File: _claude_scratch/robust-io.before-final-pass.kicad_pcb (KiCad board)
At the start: 4 copper layers, 160 x 100 mm, 304 parts, among them J1 AVR-ISP-6, J10 Screw_Terminal_01x06, J14 Screw_Terminal_01x04, J15 Screw_Terminal_01x04, J16 Screw_Terminal_01x06, J18 Screw_Terminal_01x06, J19 Screw_Terminal_01x06, J20 UART, J3 Screw_Terminal_01x06, J4 Screw_Terminal_01x04, J5 Screw_Terminal_01x06, J6 Screw_Terminal_01x06, J9 Screw_Terminal_01x06, Q3 2N7002, Q4 2N7002, SW1 CHS-01TB, SW2 B3U-1000P, U1 DRV8876, U10 BTS7008, U11 BTS7008, U14 DRV8876, U2 ATmega1284P-A, U3 MCP2515, U4 TPS5604, U5 TPS5604, U6 MCP2562-E-MF, U7 MC33978, U8 BTS7008, U9 BTS7008, Y1 16MHz, Y2 12MHz

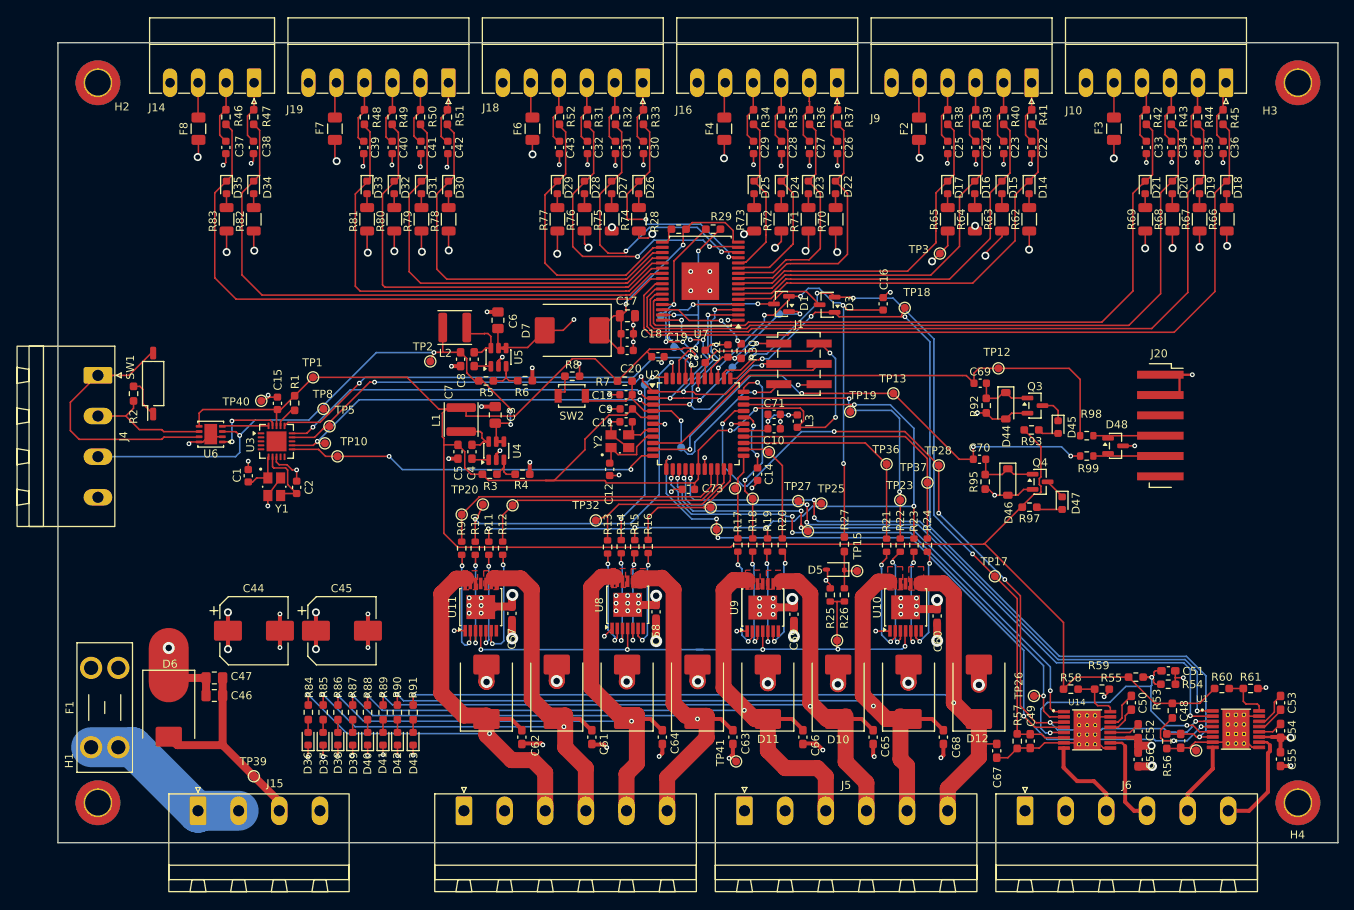
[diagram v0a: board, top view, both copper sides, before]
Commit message: Rev A: release to fab (JLCPCB, 5 PCB / 2 assembled)
Board
- Outline set to exactly 160 x 100 mm; plane zones resized to match
- UART brought out on J20 (1x6 SMD, FTDI pinout) with series
  resistors R98/R99 and TVS D48
- J1 and J20 changed to SMD headers (C52016780, C41417363)
- L1/L2 moved to Sunlord SWPA4030S footprints; regulator tracks rerouted
- 41 test points added (35 top, 6 bottom), including SPI access
- Crystal case pins (Y1/Y2 pads 2, 4) tied to GND
- SW2 changed to 2-pin push button symbol
- R84-R91 changed from 2.2k to 10k to cut dissipation at 24 V
- Thermal vias in U1/U14 enlarged to 0.3 mm drill; 27 +24V vias added
  under U8-U11; solid plane connections on high-current pins
- Input/output rows and edge connectors aligned
- /inputs/_SG4 track and via moved clear of R74 pad 1

Schematic
- ERC cleared: no-connects, PWR_FLAGs, pin types, off-grid items
- Symbols moved to project library robust-io
- Test point symbols added on processor and power sheets

Rules
- Custom DRC rule for U7 pad-to-pad clearance (0.15 mm)
- Minimum through hole 0.2 mm; silk-to-edge check ignored

Fab outputs (fab/)
- make_gerbers.sh: Gerbers, drill and position export via kicad-cli
- JLC BOM with LCSC part numbers on all 50 SMD lines
- JLC placement file with per-part rotation offsets
  (cpl_rotation_offsets.json), verified in JLC placement preview
- Through-hole BOM and test point list

DRC: 4 library-mismatch warnings (J20, U1, U14, U7), 0 errors
ERC: clean
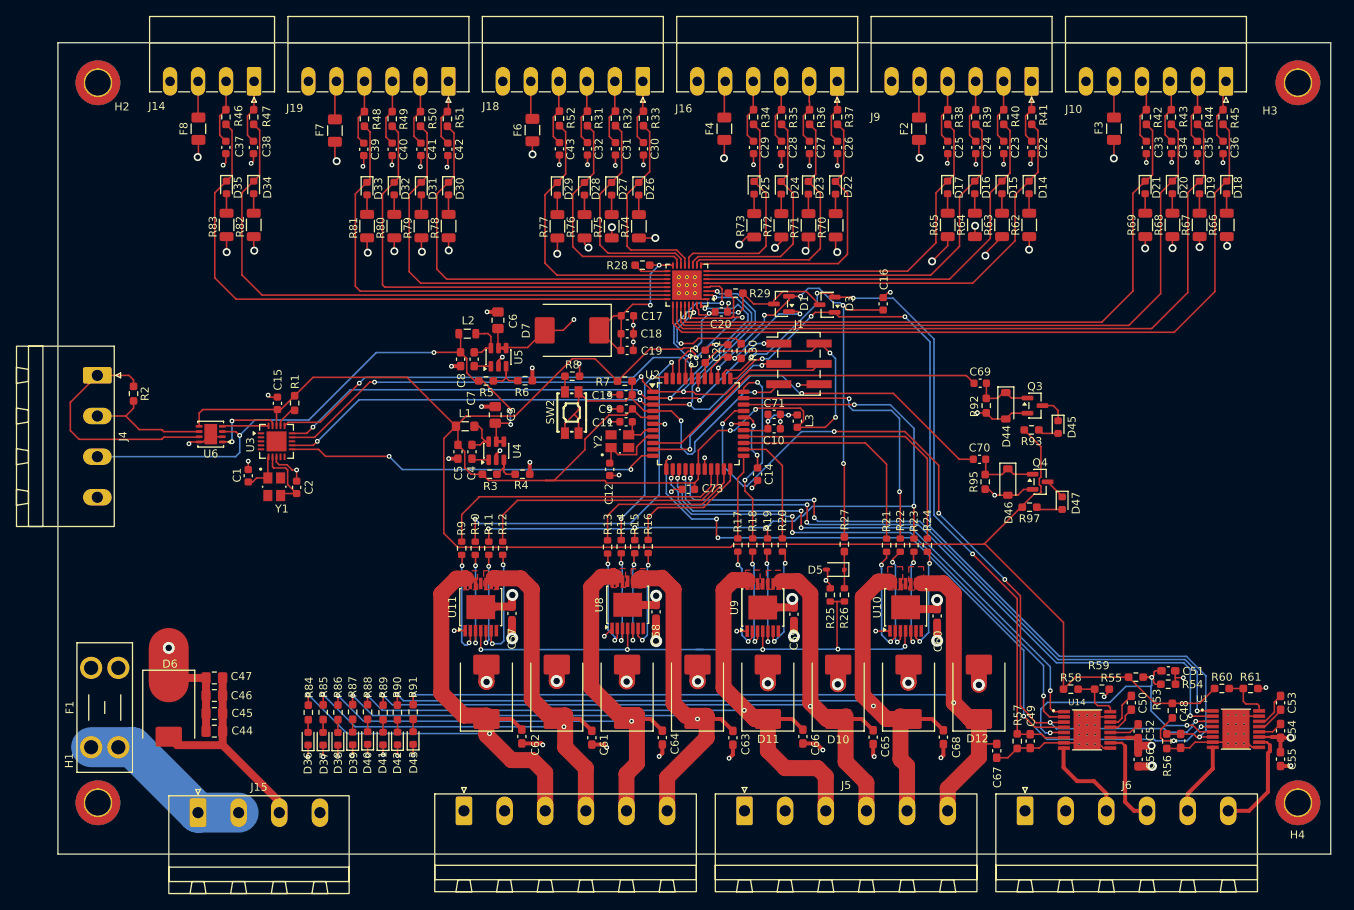
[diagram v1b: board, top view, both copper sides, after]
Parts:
- removed D48: SP0502BAHT, Package_TO_SOT_SMD:SOT-23
- removed J20: UART, Connector_PinHeader_2.54mm:PinHeader_1x06_P2.54mm_Vertical_SMD_Pin1Right
- removed R98, R99: 1k, Resistor_SMD:R_0603_1608Metric
- removed SW1: CHS-01TB, Button_Switch_SMD:SW_DIP_SPSTx01_Slide_Copal_CHS-01B_W7.62mm_P1.27mm
- removed TP1: +3.3V, TestPoint:TestPoint_Pad_D1.0mm
- removed TP10: INT_CAN0, TestPoint:TestPoint_Pad_D1.0mm
- removed TP11: RST, TestPoint:TestPoint_Pad_D1.0mm
- removed TP12: RX0, TestPoint:TestPoint_Pad_D1.0mm
- removed TP13: TX0, TestPoint:TestPoint_Pad_D1.0mm
- removed TP14: ISENSE, TestPoint:TestPoint_Pad_D1.0mm
- removed TP15: ISENSE_PROT, TestPoint:TestPoint_Pad_D1.0mm
- removed TP16: AMUX0, TestPoint:TestPoint_Pad_D1.0mm
- removed TP17: IPROPIM0, TestPoint:TestPoint_Pad_D1.0mm
- removed TP18: IPROPIM1, TestPoint:TestPoint_Pad_D1.0mm
- removed TP19: DSELn, TestPoint:TestPoint_Pad_D1.0mm
- removed TP2: +5V, TestPoint:TestPoint_Pad_D1.0mm
- removed TP20: DEN0, TestPoint:TestPoint_Pad_D1.0mm
- removed TP21: DEN1, TestPoint:TestPoint_Pad_D1.0mm
- removed TP22: DEN2, TestPoint:TestPoint_Pad_D1.0mm
- removed TP23: DEN3, TestPoint:TestPoint_Pad_D1.0mm
- removed TP24: EN_M0, TestPoint:TestPoint_Pad_D1.0mm
- removed TP25: EN_M1, TestPoint:TestPoint_Pad_D1.0mm
- removed TP26: PH_M0, TestPoint:TestPoint_Pad_D1.0mm
- removed TP27: PH_M1, TestPoint:TestPoint_Pad_D1.0mm
- removed TP28: nSLEEPMn, TestPoint:TestPoint_Pad_D1.0mm
- removed TP29: FAULTMn, TestPoint:TestPoint_Pad_D1.0mm
- removed TP3: +24V, TestPoint:TestPoint_Pad_D1.0mm
- removed TP30: DRV_OUT0, TestPoint:TestPoint_Pad_D1.0mm
- removed TP31: DRV_OUT1, TestPoint:TestPoint_Pad_D1.0mm
- removed TP32: DRV_OUT2, TestPoint:TestPoint_Pad_D1.0mm
- removed TP33: DRV_OUT3, TestPoint:TestPoint_Pad_D1.0mm
- removed TP34: DRV_OUT4, TestPoint:TestPoint_Pad_D1.0mm
- removed TP35: DRV_OUT5, TestPoint:TestPoint_Pad_D1.0mm
- removed TP36: DRV_OUT6, TestPoint:TestPoint_Pad_D1.0mm
- removed TP37: DRV_OUT7, TestPoint:TestPoint_Pad_D1.0mm
- removed TP38, TP39, TP40, TP41: GND, TestPoint:TestPoint_Pad_D1.0mm
- removed TP4: SCLK0, TestPoint:TestPoint_Pad_D1.0mm
- removed TP5: MOSI0, TestPoint:TestPoint_Pad_D1.0mm
- removed TP6: MISO0, TestPoint:TestPoint_Pad_D1.0mm
- removed TP7: CS_IN0, TestPoint:TestPoint_Pad_D1.0mm
- removed TP8: CS_CAN, TestPoint:TestPoint_Pad_D1.0mm
- removed TP9: INT_B0, TestPoint:TestPoint_Pad_D1.0mm
- C17: value 10uF 50V -> 100uF; footprint Capacitor_SMD:C_0805_2012Metric -> Capacitor_SMD:C_0603_1608Metric
- C44, C45: footprint Capacitor_SMD:CP_Elec_8x10 -> Capacitor_SMD:C_0805_2012Metric_Pad1.18x1.45mm_HandSolder
- L1: footprint Inductor_SMD:L_Sunlord_SWPA4030S -> Inductor_SMD:L_0805_2012Metric_Pad1.05x1.20mm_HandSolder
- L2: footprint Inductor_SMD:L_Sunlord_SWPA4030S -> Inductor_SMD:L_0805_2012Metric
- R84, R85, R86, R87, R88, R89, R90, R91: value 10k -> 2.2k
- SW2: value B3U-1000P -> EVQ-P9W02W; footprint Button_Switch_SMD:SW_SPST_B3U-1000P -> rml:KEY-SMD_EVQP9W02W
- U7: footprint Package_SO:HSOP-32-1EP_7.5x11mm_P0.65mm_EP4.7x4.7mm -> Package_DFN_QFN:QFN-32-1EP_5x5mm_P0.5mm_EP3.7x3.7mm_ThermalVias
- moved C45 19.0 mm to (49.5, 113.8)
- moved C44 13.5 mm to (49.5, 116.0)
- moved C20 9.70 mm to (112.9, 63.6)
- moved R29 8.48 mm to (114.7, 61.3)
- moved R28 6.39 mm to (103.1, 57.8)
- moved SW2 2.08 mm to (94.2, 76.2)
- moved U7 1.75 mm to (108.6, 60.3)
- moved L2 1.75 mm to (81.2, 66.4)
- moved L1 0.98 mm to (80.9, 77.9), turned to 180 degrees
- moved R74 0.87 mm to (102.6, 52.9)
- moved R75 0.87 mm to (99.2, 52.9)
- moved R76 0.87 mm to (95.8, 52.9)
- moved R77 0.87 mm to (92.4, 52.9)
- moved R78 0.85 mm to (78.8, 52.9)
- moved R79 0.85 mm to (75.4, 52.9)
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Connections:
- R2 pad 1: Net-(R2-Pad1) -> Net-(J4-Pin_1)
- SW2 pad 2: Net-(SW2-D) -> /processor/RST
- Y1 pad 2: GND -> unconnected-(Y1-Pad2)
- Y1 pad 4: GND -> unconnected-(Y1-Pad4)
- Y2 pad 2: GND -> unconnected-(Y2-Pad2)
- Y2 pad 4: GND -> unconnected-(Y2-Pad4)
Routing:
- net GND: track 258.0 -> 233.9 mm, vias 103 -> 91
- net /processor/RX0: track 66.4 -> 44.0 mm
- net +24V: track 131.6 -> 114.5 mm, vias 67 -> 36
- net /processor/TX0: track 64.5 -> 49.2 mm, vias 4 -> 2
- net /processor/RST: track 36.3 -> 45.6 mm
- net Net-(D7-K): track 32.8 -> 24.3 mm
- net /inputs/_SG5: track 36.5 -> 28.0 mm, vias 2 -> 0
- net +3.3V: track 366.9 -> 358.8 mm, vias 8 -> 7
- net /processor/TX0_EXT: track 7.89 -> 0.00 mm
- net /processor/RX0_EXT: track 7.89 -> 0.00 mm
- net /inputs/_SG3: track 19.8 -> 27.7 mm
- net /inputs/_SP4: track 102.3 -> 94.6 mm
- net /inputs/_SG6: track 38.6 -> 31.0 mm, vias 2 -> 0
- net /inputs/_SP5: track 97.4 -> 90.4 mm
- net /inputs/_SG2: track 23.6 -> 30.2 mm
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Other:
- board size 160 x 100 mm -> 159.1 x 101.4 mm
